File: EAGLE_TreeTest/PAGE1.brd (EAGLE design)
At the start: 160 x 100 mm, 125 parts, among them Q1 IRF640, Q2 C1815, Q3 C1815, Q4 C1815, Q5 C1815, Q6 C1815, Q7 C1815, U1 NE555_DIP8, U10 NE556, U11 4017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

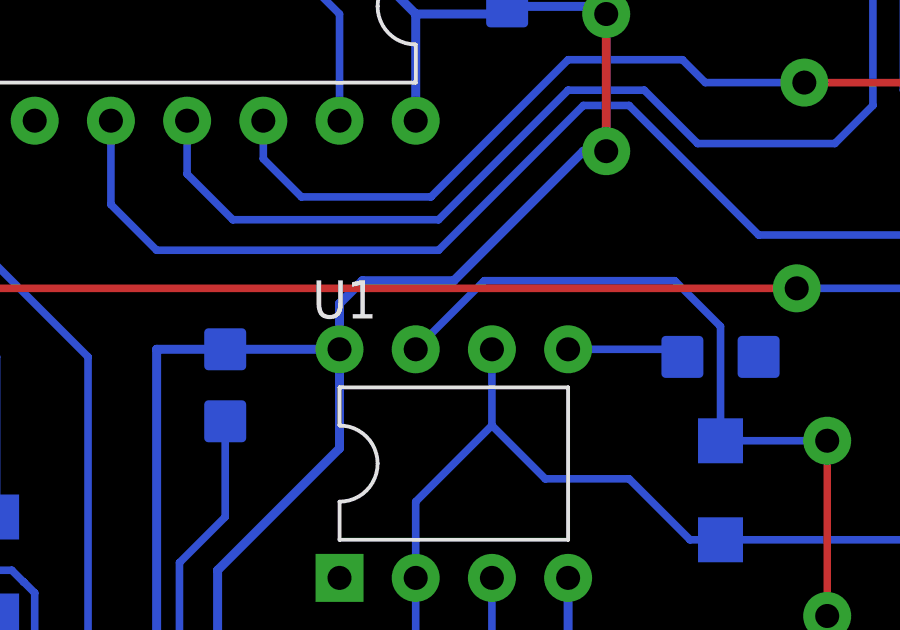
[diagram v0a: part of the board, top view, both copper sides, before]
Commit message: bottom PCB completed
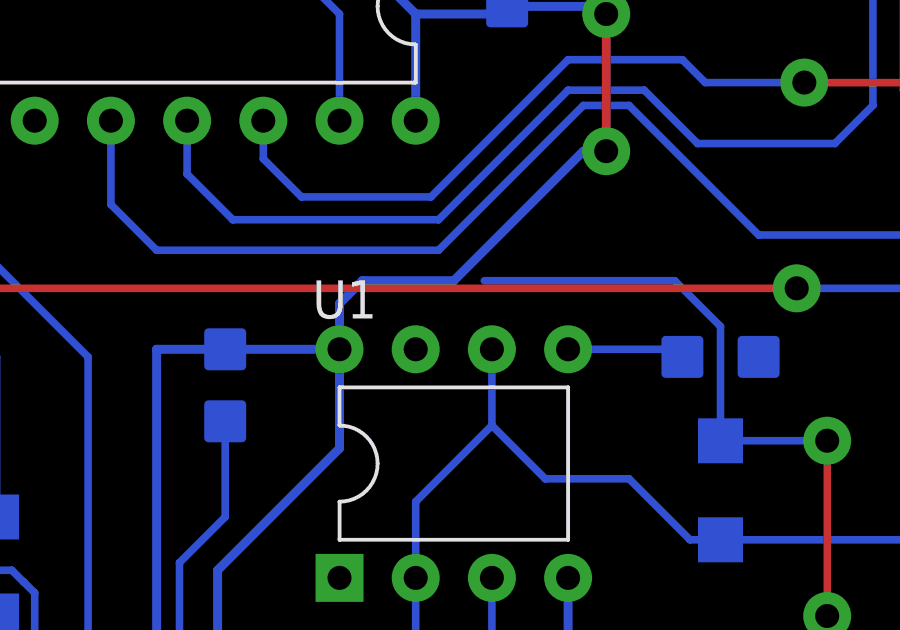
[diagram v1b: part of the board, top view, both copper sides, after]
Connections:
- net N$2: now also U1.7
- net N$3: no longer U1.7
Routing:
- net N$3: track 37.6 -> 34.4 mm
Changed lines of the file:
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@@
 <wire x1="69.596" y1="5.588" x2="71.882" y2="3.302" width="0.254" layer="16"/>
 <wire x1="71.882" y1="3.302" x2="78.74" y2="3.302" width="0.254" layer="16"/>
+<contactref element="U1" pad="7"/>
+<wire x1="71.12" y1="21.73" x2="77.47" y2="24.13" width="0" layer="19" extent="16-16"/>
 </signal>
 <signal name="N$3">
 <contactref element="D2" pad="2"/>
-<contactref element="U1" pad="7"/>
 <contactref element="VR1" pad="3"/>
-<wire x1="77.47" y1="24.13" x2="79.756" y2="26.416" width="0.254" layer="16"/>
 <wire x1="86.106" y1="26.416" x2="87.63" y2="24.892" width="0.254" layer="16"/>
 <wire x1="87.63" y1="24.892" x2="87.63" y2="21.082" width="0.254" layer="16"/>
